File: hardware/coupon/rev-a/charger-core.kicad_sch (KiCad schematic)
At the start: 6 parts, among them U41 BQ24074RGTR

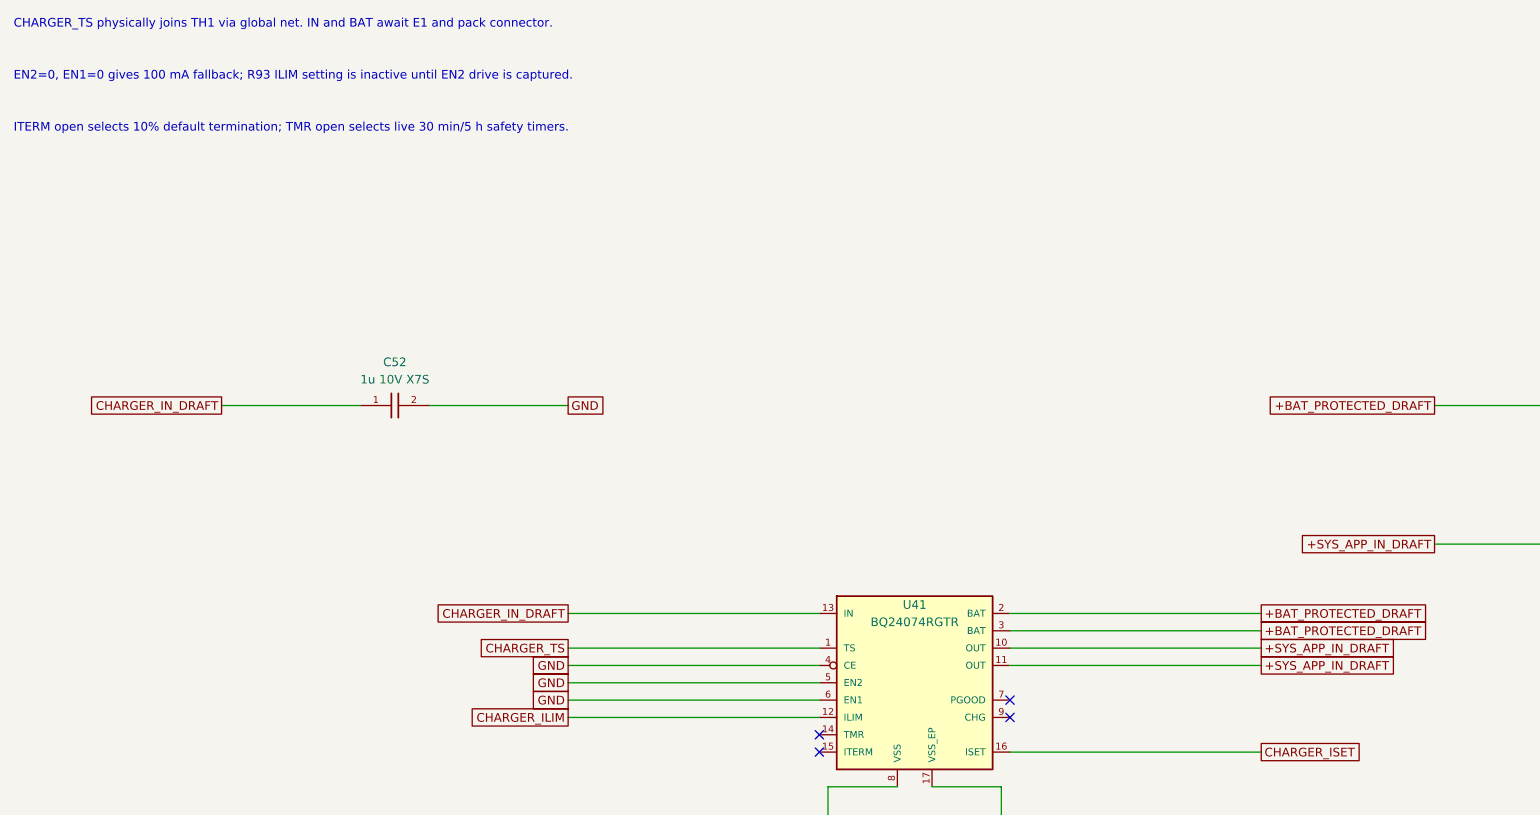
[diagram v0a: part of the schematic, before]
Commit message: Capture provisional charger EN2 clamp
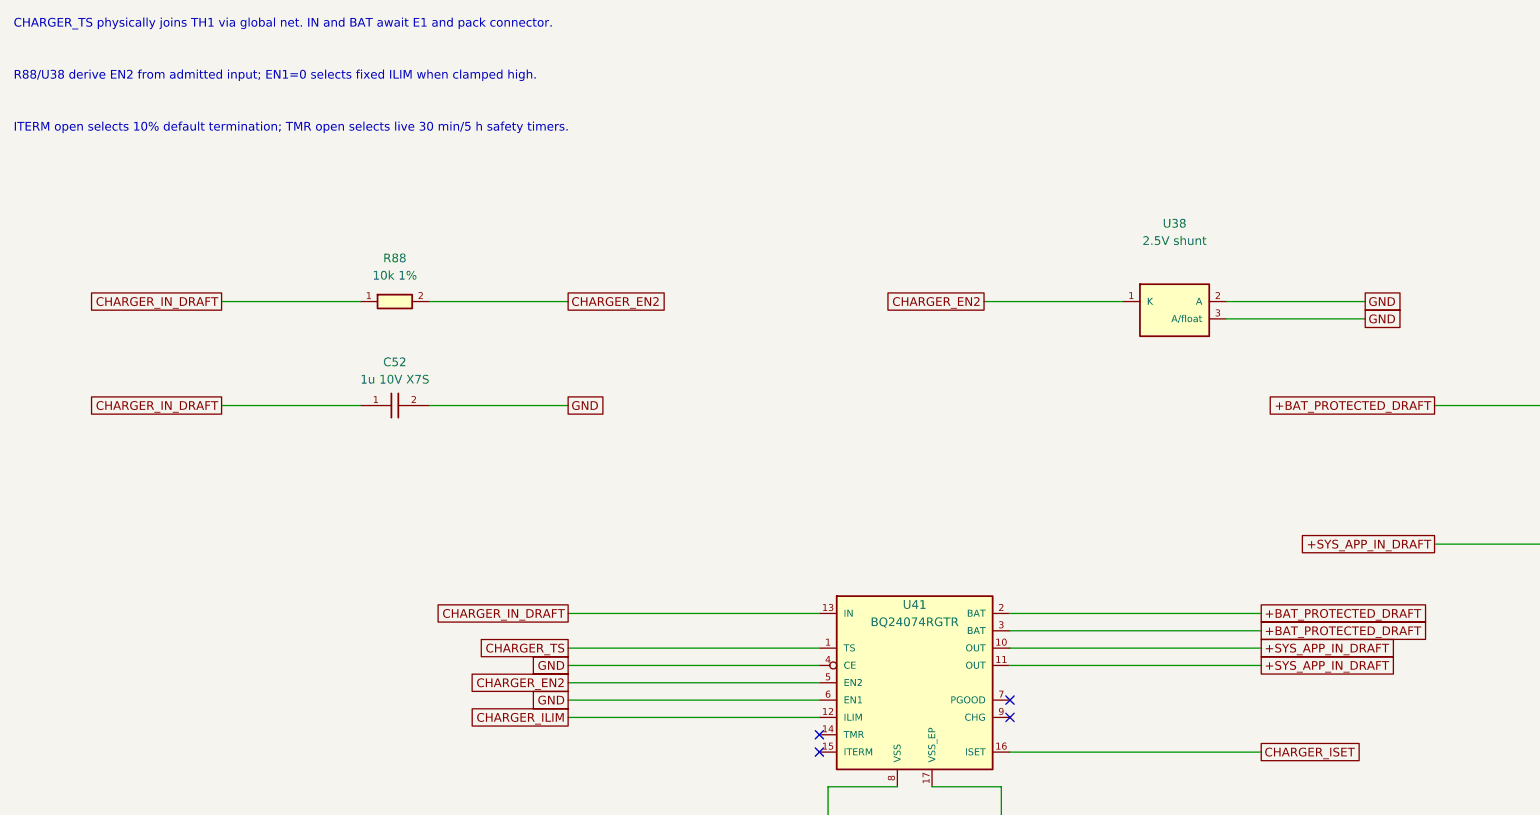
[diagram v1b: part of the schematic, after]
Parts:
- added R88: 10k 1%, rgb-badge-coupon:R_Panasonic_ERJ2_0402, symbol rgb-badge-coupon:ERJ2RKF1002X
- added U38: 2.5V shunt, rgb-badge-coupon:SOT23_TI_DBZ0003A, symbol rgb-badge-coupon:LM4040A25IDBZT
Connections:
- net CHARGER_IN_DRAFT: now also R88.1
- net GND: now also U38.2 (A), U38.3 (A/float); no longer U41.5 (EN2)
- new net CHARGER_EN2: R88.2, U38.1 (K), U41.5 (EN2)
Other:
- note added: "R88/U38 derive EN2 from admitted input; EN1=0 selects fixed ILIM when clamped high."
- note removed: "EN2=0, EN1=0 gives 100 mA fallback; R93 ILIM setting is inactive until EN2 drive is captured."
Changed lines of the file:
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@@
 (generator_version "1.0")
 (paper "A3")
-(title_block (title "Coupon Rev A - provisional BQ24074 charger core") (rev "A-draft") (comment 1 "SPDX-License-Identifier: CERN-OHL-S-2.0") (comment 2 "IN and BAT are unbuilt boundary nets; EN2 temporarily grounded"))
+(title_block (title "Coupon Rev A - provisional BQ24074 charger core") (rev "A-draft") (comment 1 "SPDX-License-Identifier: CERN-OHL-S-2.0") (comment 2 "IN and BAT are unbuilt boundary nets; EN2 uses local clamp"))
 (text "CHARGER_TS physically joins TH1 via global net. IN and BAT await E1 and pack connector." (at 20.320 20.320 0) (effects (font (size 1.27 1.27)) (justify left)))
-(text "EN2=0, EN1=0 gives 100 mA fallback; R93 ILIM setting is inactive until EN2 drive is captured." (at 20.320 27.940 0) (effects (font (size 1.27 1.27)) (justify left)))
+(text "R88/U38 derive EN2 from admitted input; EN1=0 selects fixed ILIM when clamped high." (at 20.320 27.940 0) (effects (font (size 1.27 1.27)) (justify left)))
 (text "ITERM open selects 10% default termination; TMR open selects live 30 min/5 h safety timers." (at 20.320 35.560 0) (effects (font (size 1.27 1.27)) (justify left)))
 (symbol (lib_id "rgb-badge-coupon:BQ24074RGTR") (at 152.400 116.840 0) (unit 1)
@@
 (pin "17")
 (instances (project "rgb-badge-coupon" (path "/207fb68e-2ddb-46bb-8712-eba2f8c5eef6/2f612542-2757-57f3-9ea0-8a9efdc1592b" (reference "U41") (unit 1)))))
+(symbol (lib_id "rgb-badge-coupon:ERJ2RKF1002X") (at 76.200 60.960 0) (unit 1)
+(exclude_from_sim no) (in_bom yes) (on_board yes) (dnp no)
+(property "Reference" "R88" (at 76.200 54.610 0) (effects (font (size 1.27 1.27))))
+(property "Value" "10k 1%" (at 76.200 57.150 0) (effects (font (size 1.27 1.27))))
+(property "Footprint" "rgb-badge-coupon:R_Panasonic_ERJ2_0402" (at 76.200 60.960 0) (effects (font (size 1.27 1.27)) (hide yes)))
+(property "Datasheet" "https://industrial.panasonic.com/ww/products/pt/general-purpose-chip-resistors/models/ERJ2RKF1002X" (at 76.200 60.960 0) (effects (font (size 1.27 1.27)) (hide yes)))
+(property "Manufacturer" "Panasonic" (at 76.200 60.960 0) (effects (font (size 1.27 1.27)) (hide yes)))
+(property "MPN" "ERJ2RKF1002X" (at 76.200 60.960 0) (effects (font (size 1.27 1.27)) (hide yes)))
+(pin "1")
+(pin "2")
+(instances (project "rgb-badge-coupon" (path "/207fb68e-2ddb-46bb-8712-eba2f8c5eef6/2f612542-2757-57f3-9ea0-8a9efdc1592b" (reference "R88") (unit 1)))))
+(symbol (lib_id "rgb-badge-coupon:LM4040A25IDBZT") (at 190.500 60.960 0) (unit 1)
+(exclude_from_sim no) (in_bom yes) (on_board yes) (dnp no)
+(property "Reference" "U38" (at 190.500 49.530 0) (effects (font (size 1.27 1.27))))
+(property "Value" "2.5V shunt" (at 190.500 52.070 0) (effects (font (size 1.27 1.27))))
+(property "Footprint" "rgb-badge-coupon:SOT23_TI_DBZ0003A" (at 190.500 60.960 0) (effects (font (size 1.27 1.27)) (hide yes)))
+(property "Datasheet" "https://www.ti.com/lit/ds/symlink/lm4040.pdf" (at 190.500 60.960 0) (effects (font (size 1.27 1.27)) (hide yes)))
+(property "Manufacturer" "Texas Instruments" (at 190.500 60.960 0) (effects (font (size 1.27 1.27)) (hide yes)))
+(property "MPN" "LM4040A25IDBZT" (at 190.500 60.960 0) (effects (font (size 1.27 1.27)) (hide yes)))
+(pin "1")
+(pin "2")
+(pin "3")
+(instances (project "rgb-badge-coupon" (path "/207fb68e-2ddb-46bb-8712-eba2f8c5eef6/2f612542-2757-57f3-9ea0-8a9efdc1592b" (reference "U38") (unit 1)))))
 (symbol (lib_id "rgb-badge-coupon:ERA2AEB2491X") (at 254.000 175.260 0) (unit 1)
 (exclude_from_sim no) (in_bom yes) (on_board yes) (dnp no)
@@
 (global_label "GND" (shape passive) (at 101.600 114.300 180) (effects (font (size 1.27 1.27)) (justify right)) (property "Intersheetrefs" "${INTERSHEET_REFS}" (at 101.600 114.300 0) (effects (font (size 1.27 1.27)) (hide yes))))
 (wire (pts (xy 138.430 116.840) (xy 101.600 116.840)) (stroke (width 0) (type default)))
-(global_label "GND" (shape passive) (at 101.600 116.840 180) (effects (font (size 1.27 1.27)) (justify right)) (property "Intersheetrefs" "${INTERSHEET_REFS}" (at 101.600 116.840 0) (effects (font (size 1.27 1.27)) (hide yes))))
+(global_label "CHARGER_EN2" (shape passive) (at 101.600 116.840 180) (effects (font (size 1.27 1.27)) (justify right)) (property "Intersheetrefs" "${INTERSHEET_REFS}" (at 101.600 116.840 0) (effects (font (size 1.27 1.27)) (hide yes))))
 (wire (pts (xy 138.430 119.380) (xy 101.600 119.380)) (stroke (width 0) (type default)))
 (global_label "GND" (shape passive) (at 101.600 119.380 180) (effects (font (size 1.27 1.27)) (justify right)) (property "Intersheetrefs" "${INTERSHEET_REFS}" (at 101.600 119.380 0) (effects (font (size 1.27 1.27)) (hide yes))))
@@
 (no_connect (at 138.430 124.460))
 (no_connect (at 138.430 127.000))
+(wire (pts (xy 71.120 60.960) (xy 50.800 60.960)) (stroke (width 0) (type default)))
+(global_label "CHARGER_IN_DRAFT" (shape passive) (at 50.800 60.960 180) (effects (font (size 1.27 1.27)) (justify right)) (property "Intersheetrefs" "${INTERSHEET_REFS}" (at 50.800 60.960 0) (effects (font (size 1.27 1.27)) (hide yes))))
+(wire (pts (xy 81.280 60.960) (xy 101.600 60.960)) (stroke (width 0) (type default)))
+(global_label "CHARGER_EN2" (shape passive) (at 101.600 60.960 0) (effects (font (size 1.27 1.27)) (justify left)) (property "Intersheetrefs" "${INTERSHEET_REFS}" (at 101.600 60.960 0) (effects (font (size 1.27 1.27)) (hide yes))))
+(wire (pts (xy 182.880 60.960) (xy 162.560 60.960)) (stroke (width 0) (type default)))
+(global_label "CHARGER_EN2" (shape passive) (at 162.560 60.960 180) (effects (font (size 1.27 1.27)) (justify right)) (property "Intersheetrefs" "${INTERSHEET_REFS}" (at 162.560 60.960 0) (effects (font (size 1.27 1.27)) (hide yes))))
+(wire (pts (xy 198.120 60.960) (xy 218.440 60.960)) (stroke (width 0) (type default)))
+(global_label "GND" (shape passive) (at 218.440 60.960 0) (effects (font (size 1.27 1.27)) (justify left)) (property "Intersheetrefs" "${INTERSHEET_REFS}" (at 218.440 60.960 0) (effects (font (size 1.27 1.27)) (hide yes))))
+(wire (pts (xy 198.120 63.500) (xy 218.440 63.500)) (stroke (width 0) (type default)))
+(global_label "GND" (shape passive) (at 218.440 63.500 0) (effects (font (size 1.27 1.27)) (justify left)) (property "Intersheetrefs" "${INTERSHEET_REFS}" (at 218.440 63.500 0) (effects (font (size 1.27 1.27)) (hide yes))))
 (wire (pts (xy 248.920 175.260) (xy 228.600 175.260)) (stroke (width 0) (type default)))
 (global_label "CHARGER_ISET" (shape passive) (at 228.600 175.260 180) (effects (font (size 1.27 1.27)) (justify right)) (property "Intersheetrefs" "${INTERSHEET_REFS}" (at 228.600 175.260 0) (effects (font (size 1.27 1.27)) (hide yes))))

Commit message: Capture provisional E1 charger gate with independent hardware inhibits
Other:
- note added: "CHARGER_TS joins TH1; IN joins provisional E1; BAT awaits pack connector."
- note removed: "CHARGER_TS physically joins TH1 via global net. IN and BAT await E1 and pack connector."
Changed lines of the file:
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@@
 (generator_version "1.0")
 (paper "A3")
-(title_block (title "Coupon Rev A - provisional BQ24074 charger core") (rev "A-draft") (comment 1 "SPDX-License-Identifier: CERN-OHL-S-2.0") (comment 2 "IN and BAT are unbuilt boundary nets; EN2 uses local clamp"))
-(text "CHARGER_TS physically joins TH1 via global net. IN and BAT await E1 and pack connector." (at 20.320 20.320 0) (effects (font (size 1.27 1.27)) (justify left)))
+(title_block (title "Coupon Rev A - provisional BQ24074 charger core") (rev "A-draft") (comment 1 "SPDX-License-Identifier: CERN-OHL-S-2.0") (comment 2 "IN joins provisional E1; BAT remains unbuilt; EN2 uses local clamp"))
+(text "CHARGER_TS joins TH1; IN joins provisional E1; BAT awaits pack connector." (at 20.320 20.320 0) (effects (font (size 1.27 1.27)) (justify left)))
 (text "R88/U38 derive EN2 from admitted input; EN1=0 selects fixed ILIM when clamped high." (at 20.320 27.940 0) (effects (font (size 1.27 1.27)) (justify left)))
 (text "ITERM open selects 10% default termination; TMR open selects live 30 min/5 h safety timers." (at 20.320 35.560 0) (effects (font (size 1.27 1.27)) (justify left)))
@@
 (wire (pts (xy 259.080 96.520) (xy 279.400 96.520)) (stroke (width 0) (type default)))
 (global_label "GND" (shape passive) (at 279.400 96.520 0) (effects (font (size 1.27 1.27)) (justify left)) (property "Intersheetrefs" "${INTERSHEET_REFS}" (at 279.400 96.520 0) (effects (font (size 1.27 1.27)) (hide yes))))
-(symbol (lib_id "rgb-badge-coupon:PWR_FLAG") (at 76.200 208.280 0) (unit 1)
-(exclude_from_sim no) (in_bom no) (on_board no) (dnp no)
-(property "Reference" "#FLG08" (at 76.200 203.200 0) (effects (font (size 1.27 1.27))))
-(property "Value" "PWR_FLAG" (at 76.200 205.740 0) (effects (font (size 1.27 1.27))))
-(property "Footprint" "" (at 76.200 208.280 0) (effects (font (size 1.27 1.27)) (hide yes)))
-(property "Datasheet" "" (at 76.200 208.280 0) (effects (font (size 1.27 1.27)) (hide yes)))
-(property "Manufacturer" "" (at 76.200 208.280 0) (effects (font (size 1.27 1.27)) (hide yes)))
-(property "MPN" "" (at 76.200 208.280 0) (effects (font (size 1.27 1.27)) (hide yes)))
-(pin "1")
-(instances (project "rgb-badge-coupon" (path "/207fb68e-2ddb-46bb-8712-eba2f8c5eef6/2f612542-2757-57f3-9ea0-8a9efdc1592b" (reference "#FLG08") (unit 1)))))
-(wire (pts (xy 76.200 208.280) (xy 101.600 208.280)) (stroke (width 0) (type default)))
-(global_label "CHARGER_IN_DRAFT" (shape passive) (at 101.600 208.280 0) (effects (font (size 1.27 1.27)) (justify left)) (property "Intersheetrefs" "${INTERSHEET_REFS}" (at 101.600 208.280 0) (effects (font (size 1.27 1.27)) (hide yes))))
 (symbol (lib_id "rgb-badge-coupon:PWR_FLAG") (at 254.000 208.280 0) (unit 1)
 (exclude_from_sim no) (in_bom no) (on_board no) (dnp no)

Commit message: Connect provisional protected-pack header to charger BAT
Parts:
- added J2: S2B-PH-SM4-TB, rgb-badge-coupon:JST_PH_S2B-PH-SM4-TB, symbol rgb-badge-coupon:S2B-PH-SM4-TB
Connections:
- net +BAT_PROTECTED_DRAFT: now also J2.1
- net GND: now also J2.2
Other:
- note added: "CHARGER_TS joins TH1; IN joins E1; J2 pad 1 is BAT+, pad 2 GND. Check/repin pack before mating."
- note removed: "CHARGER_TS joins TH1; IN joins provisional E1; BAT awaits pack connector."
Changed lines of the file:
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@@
 (generator_version "1.0")
 (paper "A3")
-(title_block (title "Coupon Rev A - provisional BQ24074 charger core") (rev "A-draft") (comment 1 "SPDX-License-Identifier: CERN-OHL-S-2.0") (comment 2 "IN joins provisional E1; BAT remains unbuilt; EN2 uses local clamp"))
-(text "CHARGER_TS joins TH1; IN joins provisional E1; BAT awaits pack connector." (at 20.320 20.320 0) (effects (font (size 1.27 1.27)) (justify left)))
+(title_block (title "Coupon Rev A - provisional BQ24074 charger core") (rev "A-draft") (comment 1 "SPDX-License-Identifier: CERN-OHL-S-2.0") (comment 2 "IN joins provisional E1; J2 polarity must be verified before mating; EN2 local clamp"))
+(text "CHARGER_TS joins TH1; IN joins E1; J2 pad 1 is BAT+, pad 2 GND. Check/repin pack before mating." (at 20.320 20.320 0) (effects (font (size 1.27 1.27)) (justify left)))
 (text "R88/U38 derive EN2 from admitted input; EN1=0 selects fixed ILIM when clamped high." (at 20.320 27.940 0) (effects (font (size 1.27 1.27)) (justify left)))
 (text "ITERM open selects 10% default termination; TMR open selects live 30 min/5 h safety timers." (at 20.320 35.560 0) (effects (font (size 1.27 1.27)) (justify left)))
+(symbol (lib_id "rgb-badge-coupon:S2B-PH-SM4-TB") (at 254.000 214.630 0) (unit 1)
+(exclude_from_sim no) (in_bom yes) (on_board yes) (dnp no)
+(property "Reference" "J2" (at 274.320 212.090 0) (effects (font (size 1.27 1.27))))
+(property "Value" "S2B-PH-SM4-TB" (at 274.320 217.170 0) (effects (font (size 1.27 1.27))))
+(property "Footprint" "rgb-badge-coupon:JST_PH_S2B-PH-SM4-TB" (at 254.000 214.630 0) (effects (font (size 1.27 1.27)) (hide yes)))
+(property "Datasheet" "https://www.jst-mfg.com/product/pdf/eng/ePH.pdf" (at 254.000 214.630 0) (effects (font (size 1.27 1.27)) (hide yes)))
+(property "Manufacturer" "JST" (at 254.000 214.630 0) (effects (font (size 1.27 1.27)) (hide yes)))
+(property "MPN" "S2B-PH-SM4-TB" (at 254.000 214.630 0) (effects (font (size 1.27 1.27)) (hide yes)))
+(pin "1")
+(pin "2")
+(instances (project "rgb-badge-coupon" (path "/207fb68e-2ddb-46bb-8712-eba2f8c5eef6/2f612542-2757-57f3-9ea0-8a9efdc1592b" (reference "J2") (unit 1)))))
 (symbol (lib_id "rgb-badge-coupon:BQ24074RGTR") (at 152.400 116.840 0) (unit 1)
 (exclude_from_sim no) (in_bom yes) (on_board yes) (dnp no)
@@
 (wire (pts (xy 259.080 96.520) (xy 279.400 96.520)) (stroke (width 0) (type default)))
 (global_label "GND" (shape passive) (at 279.400 96.520 0) (effects (font (size 1.27 1.27)) (justify left)) (property "Intersheetrefs" "${INTERSHEET_REFS}" (at 279.400 96.520 0) (effects (font (size 1.27 1.27)) (hide yes))))
-(symbol (lib_id "rgb-badge-coupon:PWR_FLAG") (at 254.000 208.280 0) (unit 1)
+(wire (pts (xy 246.380 212.090) (xy 220.980 212.090)) (stroke (width 0) (type default)))
+(global_label "+BAT_PROTECTED_DRAFT" (shape passive) (at 220.980 212.090 180) (effects (font (size 1.27 1.27)) (justify right)) (property "Intersheetrefs" "${INTERSHEET_REFS}" (at 220.980 212.090 0) (effects (font (size 1.27 1.27)) (hide yes))))
+(wire (pts (xy 246.380 217.170) (xy 220.980 217.170)) (stroke (width 0) (type default)))
+(global_label "GND" (shape passive) (at 220.980 217.170 180) (effects (font (size 1.27 1.27)) (justify right)) (property "Intersheetrefs" "${INTERSHEET_REFS}" (at 220.980 217.170 0) (effects (font (size 1.27 1.27)) (hide yes))))
+(symbol (lib_id "rgb-badge-coupon:PWR_FLAG") (at 254.000 233.680 0) (unit 1)
 (exclude_from_sim no) (in_bom no) (on_board no) (dnp no)
-(property "Reference" "#FLG09" (at 254.000 203.200 0) (effects (font (size 1.27 1.27))))
-(property "Value" "PWR_FLAG" (at 254.000 205.740 0) (effects (font (size 1.27 1.27))))
-(property "Footprint" "" (at 254.000 208.280 0) (effects (font (size 1.27 1.27)) (hide yes)))
-(property "Datasheet" "" (at 254.000 208.280 0) (effects (font (size 1.27 1.27)) (hide yes)))
-(property "Manufacturer" "" (at 254.000 208.280 0) (effects (font (size 1.27 1.27)) (hide yes)))
-(property "MPN" "" (at 254.000 208.280 0) (effects (font (size 1.27 1.27)) (hide yes)))
+(property "Reference" "#FLG09" (at 254.000 228.600 0) (effects (font (size 1.27 1.27))))
+(property "Value" "PWR_FLAG" (at 254.000 231.140 0) (effects (font (size 1.27 1.27))))
+(property "Footprint" "" (at 254.000 233.680 0) (effects (font (size 1.27 1.27)) (hide yes)))
+(property "Datasheet" "" (at 254.000 233.680 0) (effects (font (size 1.27 1.27)) (hide yes)))
+(property "Manufacturer" "" (at 254.000 233.680 0) (effects (font (size 1.27 1.27)) (hide yes)))
+(property "MPN" "" (at 254.000 233.680 0) (effects (font (size 1.27 1.27)) (hide yes)))
 (pin "1")
 (instances (project "rgb-badge-coupon" (path "/207fb68e-2ddb-46bb-8712-eba2f8c5eef6/2f612542-2757-57f3-9ea0-8a9efdc1592b" (reference "#FLG09") (unit 1)))))
-(wire (pts (xy 254.000 208.280) (xy 279.400 208.280)) (stroke (width 0) (type default)))
-(global_label "+BAT_PROTECTED_DRAFT" (shape passive) (at 279.400 208.280 0) (effects (font (size 1.27 1.27)) (justify left)) (property "Intersheetrefs" "${INTERSHEET_REFS}" (at 279.400 208.280 0) (effects (font (size 1.27 1.27)) (hide yes))))
+(wire (pts (xy 254.000 233.680) (xy 279.400 233.680)) (stroke (width 0) (type default)))
+(global_label "+BAT_PROTECTED_DRAFT" (shape passive) (at 279.400 233.680 0) (effects (font (size 1.27 1.27)) (justify left)) (property "Intersheetrefs" "${INTERSHEET_REFS}" (at 279.400 233.680 0) (effects (font (size 1.27 1.27)) (hide yes))))
 (embedded_fonts no)
 )
